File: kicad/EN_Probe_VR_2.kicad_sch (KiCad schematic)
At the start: 25 parts, among them J2 I2C-IN, J3 I2C-Device, J4 AUDIO OUT, J5 MEMS MIC, U1 3.3V REG, U2 2.8V REG

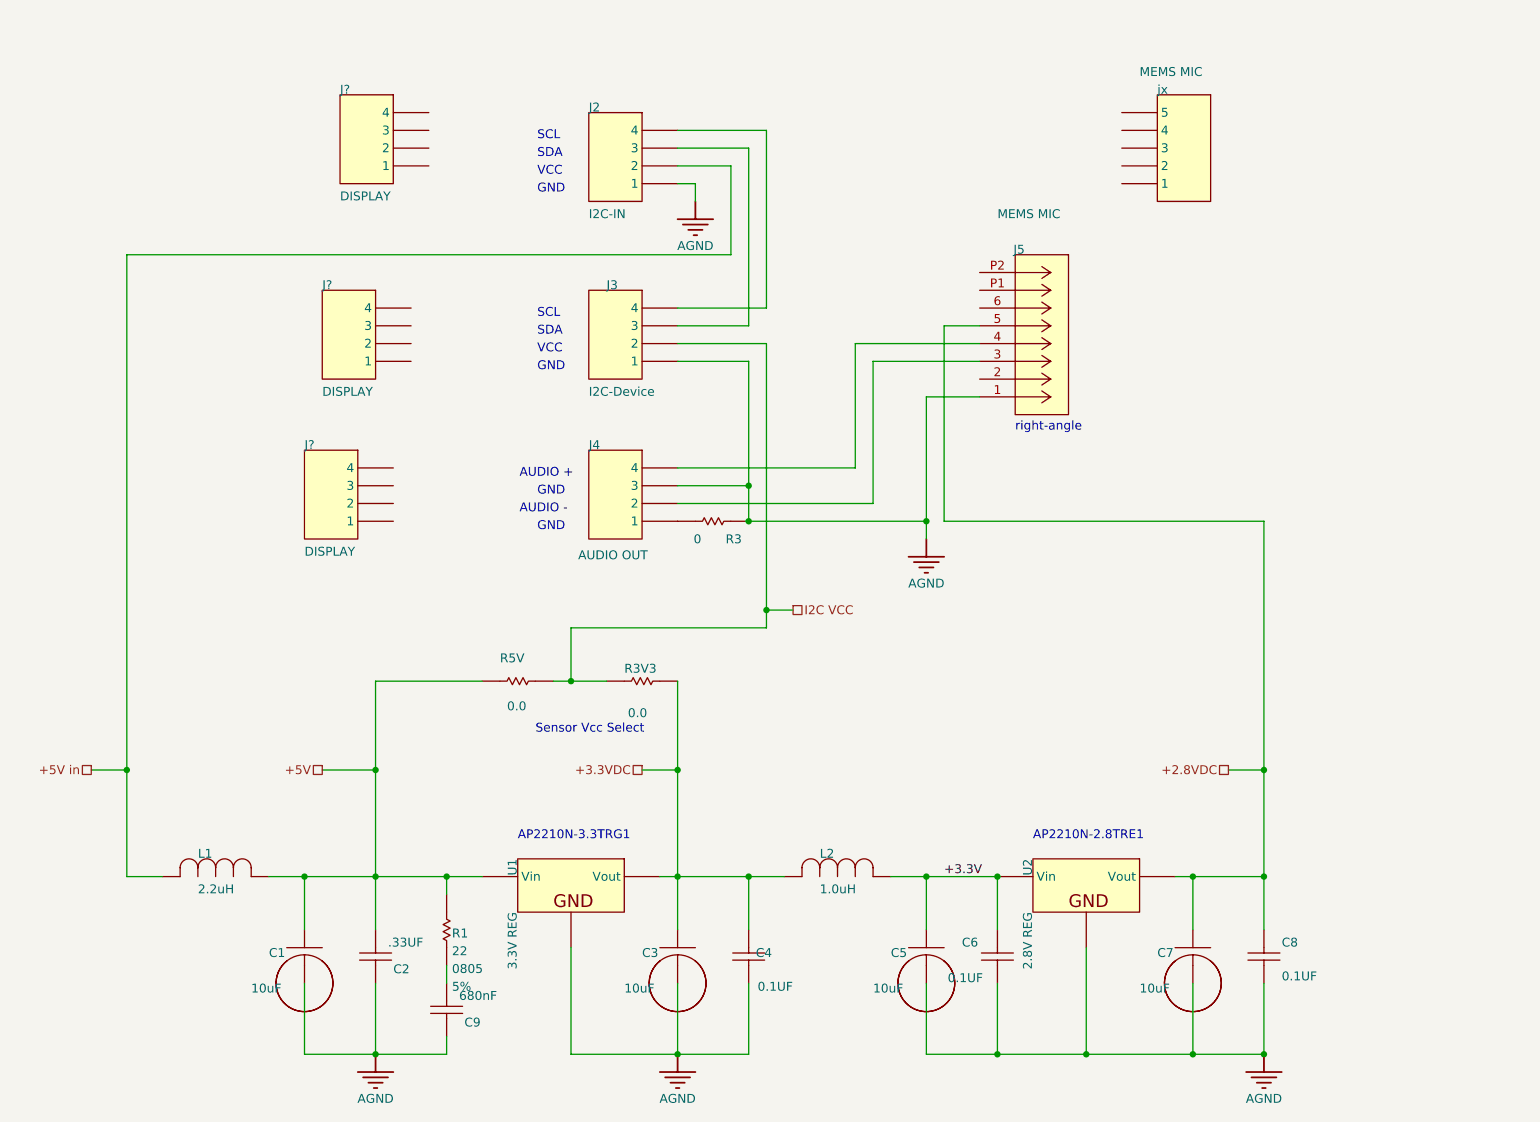
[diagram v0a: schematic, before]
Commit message: EN_Probe_VR rev 2.00: verified KiCad conversion + ver 2.00 implementation
Goal 1 - conversion audit: verified the Altium->KiCad 10 conversion against the
Altium originals and repaired it: rebuilt footprint<->symbol links, created project
symbol/footprint libraries, converted ports to global labels, added power flags,
and resolved the value/MPN conflicts the Altium project carried internally
(C9 0.33uF, ferrite beads relabelled, U1 MPN, 0R jumpers). Closed with a
zero-mismatch schematic<->PCB cross-check.

Goal 2 - rev 2.00 implementation: new 34.925 x 25.4 mm outline, M2 mounting
holes, 2.54 mm headers with J3 reordered (SDA/SCL/GND/VCC), audio output RC
coupling (220R + 0.33uF + 39k per leg, fc ~12 Hz), 10k I2C pull-ups, 100 nF mic
bypass at the ZIF, solid two-layer ground, fully re-routed. Mic connector
corrected to the 8-circuit Molex 52745-0897 (the Infineon flex tail is 8 fingers
/ 4.5 mm and cannot enter the 6-circuit part; pinout: 2/7 GND, 4 OUT-, 5 OUT+,
6 VDD). Sensor VCC defaults to 3.3 V (R2 DNP, fit exactly one of R2/R3V3).

ERC 0/0, DRC 0, schematic parity 0, unconnected 0. Do not fabricate until the
flex continuity check confirms the connector pin mapping (V<->6, P<->5, N<->4,
G<->2 and 7 on a physical flex).
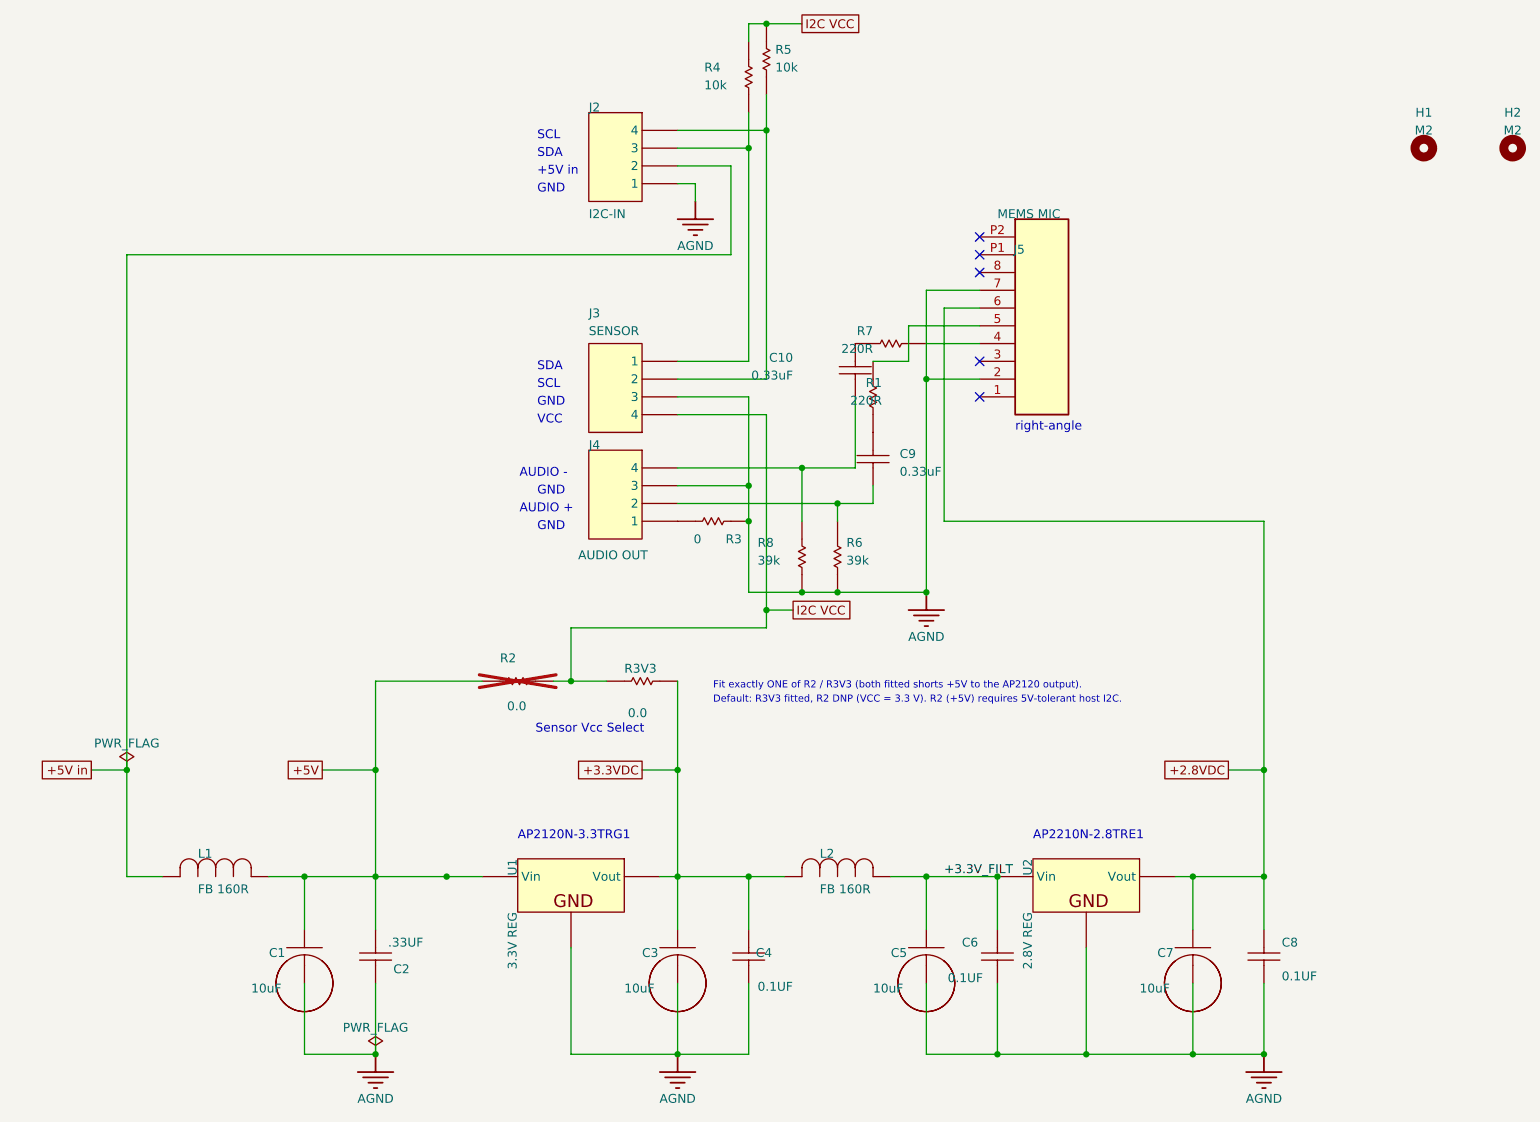
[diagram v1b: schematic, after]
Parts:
- removed J? (x3): DISPLAY, HDR1X4, symbol SC MINI_Merge Phono 3.3 60:Header 4
- removed jx: MEMS MIC, HDR1X5, symbol altium:CONN1X5
- added C10: 0.33uF, EN_Probe_VR_2:C_0805_2012Metric, symbol EN_Probe_VR_2:CAP
- added H1, H2: M2, EN_Probe_VR_2:MountingHole_2.2mm_M2, symbol Mechanical:MountingHole
- added R4, R5: 10k, EN_Probe_VR_2:R_0805_2012Metric, symbol EN_Probe_VR_2:R_0805
- added R6, R8: 39k, EN_Probe_VR_2:R_0805_2012Metric, symbol EN_Probe_VR_2:R_0805
- added R7: 220R, EN_Probe_VR_2:R_0805_2012Metric, symbol EN_Probe_VR_2:R_0805
- C1, C3, C5, C7: footprint 0805 -> EN_Probe_VR_2:C_0805_2012Metric; symbol *:CAPACITOR -> EN_Probe_VR_2:CAPACITOR
- C2: footprint 0805 -> EN_Probe_VR_2:C_0805_2012Metric; symbol *:CAP -> EN_Probe_VR_2:CAP
- C4, C6, C8: footprint 0603 -> EN_Probe_VR_2:C_0603_1608Metric; symbol *:CAP -> EN_Probe_VR_2:CAP
- C9: value 680nF -> 0.33uF; footprint 0805 -> EN_Probe_VR_2:C_0805_2012Metric; symbol *:CAP -> EN_Probe_VR_2:CAP
- J2, J4: footprint HDRA1X4 2MM -> EN_Probe_VR_2:PinHeader_1x04_P2.54mm_Vertical; symbol Miscellaneous Connectors:Header 4 -> EN_Probe_VR_2:Header_4
- J3: value I2C-Device -> SENSOR; footprint HDRA1X4 2MM -> EN_Probe_VR_2:PinHeader_1x04_P2.54mm_Vertical; symbol Miscellaneous Connectors:Header 4 -> EN_Probe_VR_2:Header_4
- J5: footprint (none) -> EN_Probe_VR_2:CON_527450897; symbol 527450697:527450697 -> EN_Probe_VR_2:CON_527450897; MANUFACTURER_PART_NUMBER 527450697 -> 527450897
- L1: value 2.2uH -> FB 160R; footprint 1206 -> EN_Probe_VR_2:1206; symbol 2020-08-13_00-23-02:HI1206T161R-10 -> EN_Probe_VR_2:FB_HI1206T161R-10
- L2: value 1.0uH -> FB 160R; footprint 1206 -> EN_Probe_VR_2:1206; symbol 2020-08-13_00-23-02:HI1206T161R-10 -> EN_Probe_VR_2:FB_HI1206T161R-10
- R1: value CRCW080522R0JNEA -> 220R; footprint 0805 -> EN_Probe_VR_2:R_0805_2012Metric; symbol SugarCube SCADng_R3.1 40:CRCW080522R0JNEA -> EN_Probe_VR_2:R_0805; ALTIUM_VALUE 22 -> 220; PARTNUMBER CRCW080522R0JNEA -> (none); RES_OHM 22 -> 220; SUPPLIER PART NUMBER 1 541-22ACT-ND -> (none); SUPPLIER PART NUMBER 2 59M6875 -> (none); SUPPLIER PART NUMBER 3 71-CRCW080522R0JNEA -> (none); VALUE_CODE 22R0 -> 220R
- R2: renamed from R5V; value CRCW080522R0JNEA -> 0R; footprint 0805 -> EN_Probe_VR_2:R_0805_2012Metric; symbol SugarCube SCADng_R3.1 40:CRCW080522R0JNEA -> EN_Probe_VR_2:R_0805; PARTNUMBER CRCW080522R0JNEA -> (none); SUPPLIER PART NUMBER 1 541-22ACT-ND -> (none); SUPPLIER PART NUMBER 2 59M6875 -> (none); SUPPLIER PART NUMBER 3 71-CRCW080522R0JNEA -> (none); VALUE_CODE 22R0 -> 0R0; now not fitted
- R3, R3V3: value CRCW080522R0JNEA -> 0R; footprint 0805 -> EN_Probe_VR_2:R_0805_2012Metric; symbol SugarCube SCADng_R3.1 40:CRCW080522R0JNEA -> EN_Probe_VR_2:R_0805; PARTNUMBER CRCW080522R0JNEA -> (none); SUPPLIER PART NUMBER 1 541-22ACT-ND -> (none); SUPPLIER PART NUMBER 2 59M6875 -> (none); SUPPLIER PART NUMBER 3 71-CRCW080522R0JNEA -> (none); VALUE_CODE 22R0 -> 0R0
- U1: footprint SOT23-3 -> EN_Probe_VR_2:SOT23-3; symbol EN_Probe_VR:Volt Reg -> EN_Probe_VR_2:Volt_Reg; MANUFACTURER PART NUMBER 1 AP2210N-2.8TRE1 -> AP2120N-3.3TRG1; SUPPLIER PART NUMBER 1 AP2210N-2.8TRE1-ND -> AP2120N-3.3TRG1DICT-ND; SUPPLIER PART NUMBER 2 MC78M12CDTRKGOSCT-ND -> (none)
- U2: footprint SOT23-3 -> EN_Probe_VR_2:SOT23-3; symbol EN_Probe_VR:Volt Reg -> EN_Probe_VR_2:Volt_Reg; SUPPLIER PART NUMBER 2 MC78M12CDTRKGOSCT-ND -> (none)
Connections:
- net +2.8VDC: now also J5.6; no longer J5.5
- net +5V: no longer R1.2
- net AGND: now also J3.3, J5.2, J5.7, R6.2, R8.2; no longer C9.1, J3.1, J5.1
- net I2C VCC: now also J3.4, R4.1, R5.1; no longer J3.2
- net at J4.2: now also C9.1, R6.1; no longer J5.3
- net at J4.4: now also C10.2, R8.1; no longer J5.4
- net at C9.2: now also R1.2; no longer R1.1
- net at J2.3: now also J3.1, R4.2; no longer J3.3
- net at J2.4: now also J3.2, R5.2; no longer J3.4
- net +3.3V renamed +3.3V_FILT
- new net: C10.1, R7.1
- new net: J5.4, R7.2
- new net: J5.5, R1.1
- no-connect marks 0 -> 5
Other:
- note added: "+5V in"
- note added: "AP2120N-3.3TRG1"
- note added: "Default: R3V3 fitted, R2 DNP (VCC = 3.3 V). R2 (+5V) requires 5V-tolerant host I2C."
- note added: "Fit exactly ONE of R2 / R3V3 (both fitted shorts +5V to the AP2120 output)."
- note removed: "AP2210N-3.3TRG1"
- title: (none) -> EN_Probe_VR
- moved on the sheet: C9, J3, R1

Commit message: Per owner review: R2 no longer DNP - both VCC-select jumpers are normal parts; per-build choice marked DNI on the BOM; schematic note updated
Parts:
- R2: now fitted
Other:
- note added: "Populate ONE per build; mark the other DNI on the BOM. R2 (+5V) requires 5V-tolerant host I2C."
- note removed: "Default: R3V3 fitted, R2 DNP (VCC = 3.3 V). R2 (+5V) requires 5V-tolerant host I2C."
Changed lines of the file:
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@@
 		)
 	)
-	(text "Default: R3V3 fitted, R2 DNP (VCC = 3.3 V). R2 (+5V) requires 5V-tolerant host I2C."
+	(text "Populate ONE per build; mark the other DNI on the BOM. R2 (+5V) requires 5V-tolerant host I2C."
 		(exclude_from_sim no)
 		(at 190.5 155.702 0)
@@
 		(on_board yes)
 		(in_pos_files yes)
-		(dnp yes)
+		(dnp no)
 		(property "Reference" "R2"
 			(at 160.02 149.86 90)
